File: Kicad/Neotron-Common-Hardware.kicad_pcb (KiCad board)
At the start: 4 copper layers, 243.8 x 243.8 mm, 197 parts, among them J1001 SD_Card, J201 DE15HD, J301 RJ45_Amphenol_RJMG1BD3B8K1ANR, J401 CD Audio In, J402 AC'97 Audio Header, J403 Line Out, J501 USB Ports External, J502 USB Ports Internal, J601 Jack-DC, J602 Conn_01x04, J603 Double-mini-DIN-6, J801 Conn_02x05, J802 DB9_Male_MountingHoles, J901 DB9_Female_MountingHoles, SW601 SW_DIP_x01, SW602 SW_DIP_x01, U201 TPF133A, U202 TPD7S019, U301 ENC424J600-PT, U401 TLV320AIC23BPW, U402 STX-4335-5BGP-S1, U501 AP2501, U502 MIC2005A-2YM5, U503 MIC2005A-2YM5, U504 XR22404CG28, U505 MIC2005A-2YM5, U506 MIC2005A-2YM5, U601 K7805-3AR3, U602 AMS1117CD-3.3, U603 MAX1615xUK, U604 MKE04P24M48SF0, U801 ST3232CDR, Y301 25M, Y401 12M, Y501 12M

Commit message: Updated PCB
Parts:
- C601, C602: value 100u -> 100u 50V
- C606: value 1u -> 1u 50V
- F601: value 5A Polyfuse -> 6A PTC; footprint Fuse:Fuse_Littelfuse_395Series -> Fuse:Fuse_Bourns_MF-RG500
- J301: value RJ45_Amphenol_RJMG1BD3B8K1ANR -> RJ45 MagJack
- R209: value DNP -> DNF
- U201: value TPF133A -> THS7316
- U301: value ENC424J600-PT -> ENC424J600
- U601: value K7805-3AR3 -> 5V DC-DC Module
- U602: value AMS1117CD-3.3 -> 3v3 LDO
- U603: value MAX1615xUK -> MAX1615
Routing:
- net Net-(U504-Pad21): track 0.00 -> 1.24 mm, vias 0 -> 1
- net (no net): track 1.24 -> 0.00 mm, vias 1 -> 0

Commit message: Make CPU card bigger.
Just big enough to take a TQFP-176 now.
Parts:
- removed J901: DB9_Female_MountingHoles, Connector_Dsub:DSUB-9_Female_Horizontal_P2.77x2.84mm_EdgePinOffset4.94mm_Housed_MountingHolesOffset7.48mm
- removed R505: 100k, Resistor_SMD:R_0805_2012Metric_Pad1.15x1.40mm_HandSolder
- added C511: 4u7, Capacitor_THT:CP_Radial_D6.3mm_P2.50mm, F.Cu at (117.1, 50.2)
- added R507: 10k, Resistor_SMD:R_0805_2012Metric_Pad1.15x1.40mm_HandSolder, F.Cu at (124.6, 50.7)
- added R508: 10k, Resistor_SMD:R_0805_2012Metric_Pad1.15x1.40mm_HandSolder, F.Cu at (123.9, 42.6)
- added R509: 10k, Resistor_SMD:R_0805_2012Metric_Pad1.15x1.40mm_HandSolder, F.Cu at (124.6, 53.7)
- added U101: Neotron-CPU, Neotron-Common-Hardware:Neotron_CPU_Socket, F.Cu at (252.2, 163.3)
- moved C508 131.5 mm to (124.6, 47.8)
- moved C801 1.27 mm to (196.8, 70.5)
- moved J601 0.51 mm to (252.2, 43.4)
- moved U505 0.32 mm to (257.2, 62.9)
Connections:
- net /Video/BLUE renamed /Video/BLUE_ANA
- net /Video/GREEN renamed /Video/GREEN_ANA
- net /Video/RED renamed /Video/RED_ANA
- C508 pad 1: Net-(C508-Pad1) -> /USB/USB_3V3
- R504 pad 1: /USB/USB_5V -> /USB/USB_3V3
- R504 pad 2: Net-(C508-Pad1) -> Net-(R504-Pad2)
- U504 pad 17: (no net) -> Net-(R504-Pad2)
- U504 pad 18: Net-(C508-Pad1) -> Net-(R508-Pad2)
- U504 pad 19: +3V3 -> Net-(R507-Pad2)
- U504 pad 21: (no net) -> /USB/USB_3V3
- U504 pad 27: +3V3 -> Net-(R509-Pad2)
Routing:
- net +3V3: track 4.74 -> 0.11 mm, vias 3 -> 0
- net GND: track 2.08 -> 0.00 mm, vias 1 -> 0
- net Net-(R507-Pad2): track 0.00 -> 1.24 mm, vias 0 -> 1
- net Net-(U504-Pad21): track 1.24 -> 0.00 mm, vias 1 -> 0
- net Net-(R509-Pad2): track 0.00 -> 1.24 mm, vias 0 -> 1
- net /USB/USB_3V3: track 0.00 -> 1.24 mm, vias 0 -> 1
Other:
- board text added: "DC In"
- board text added: "Ethernet"
- board text removed: "Ethernet 100base-T"

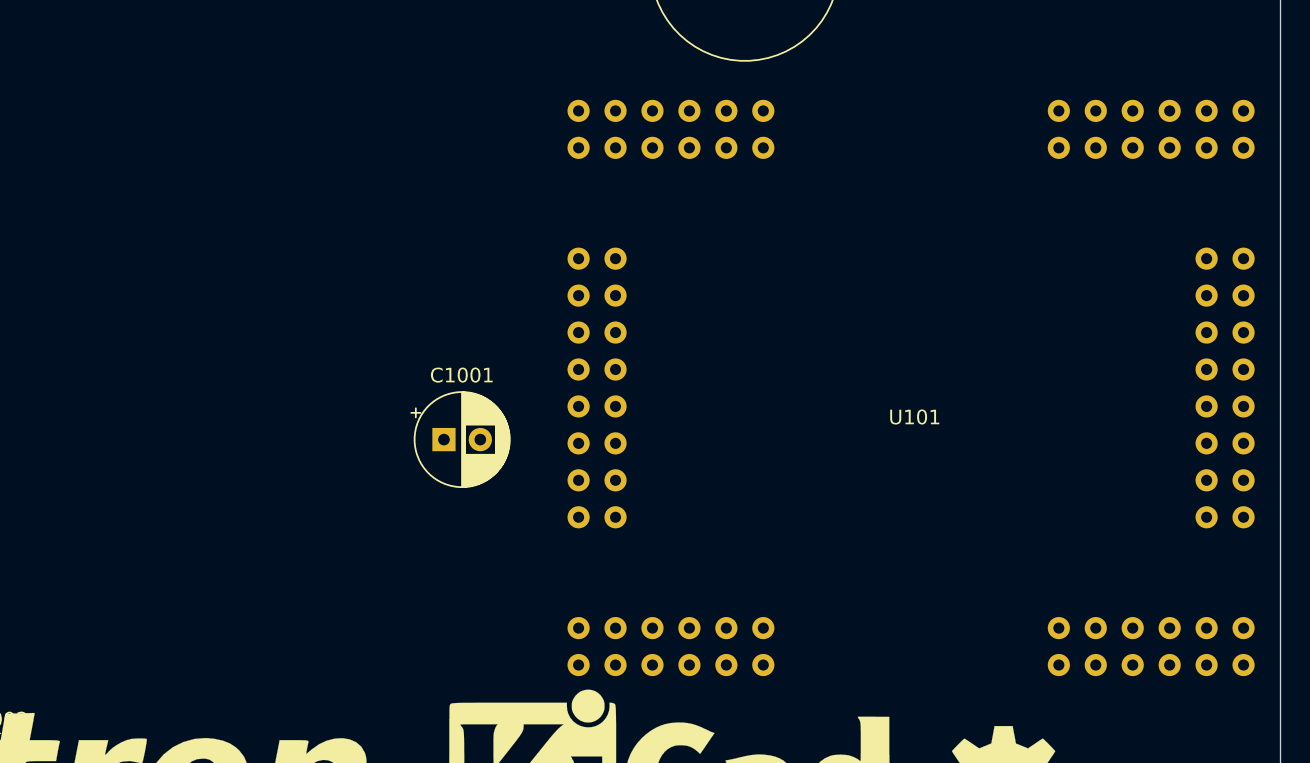
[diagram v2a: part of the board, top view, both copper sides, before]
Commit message: Revised CPU connector to be two 2x20.
This gives more room for larger TQFP-176+ CPUs to be fitted that
didn't fit on the PGA-80 design.
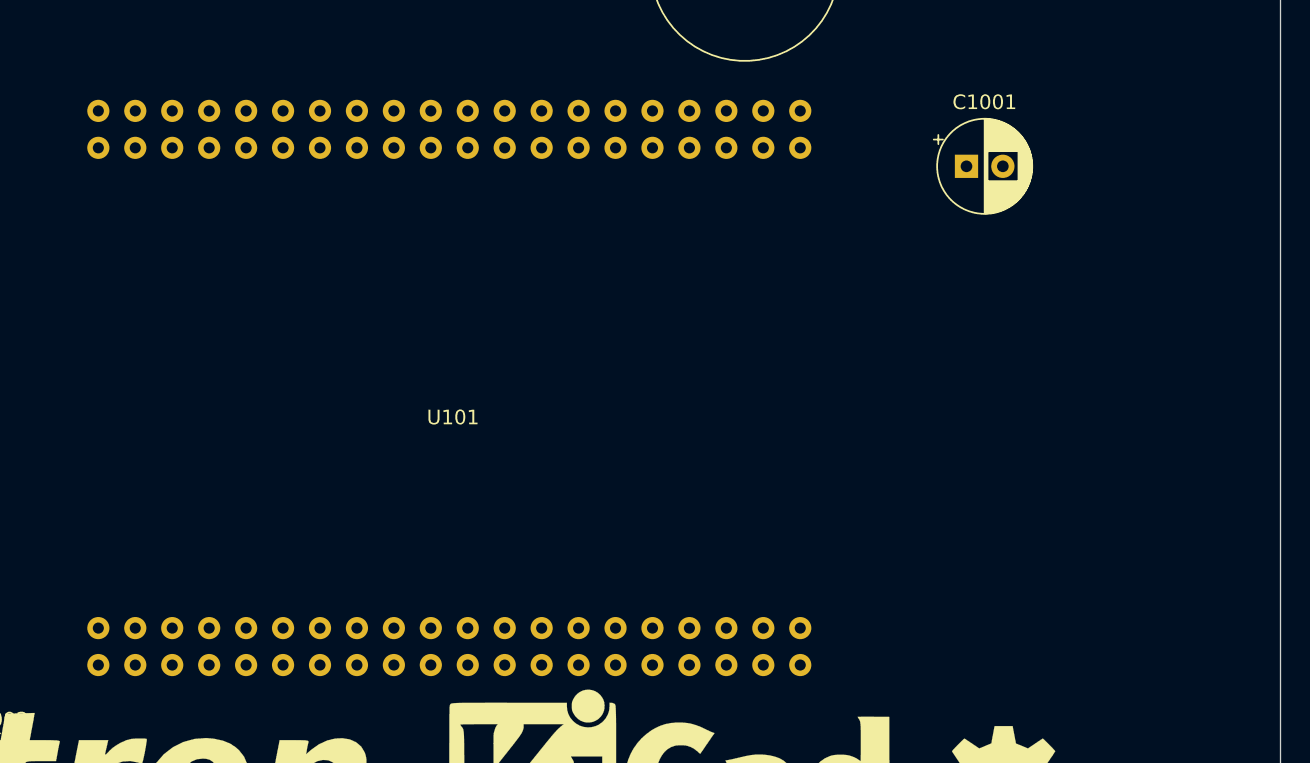
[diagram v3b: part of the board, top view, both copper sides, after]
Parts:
- moved C1001 40.5 mm to (256.0, 148.0)
- moved U101 31.8 mm to (220.4, 163.3)
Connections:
- net /Ethernet/~INT renamed /Ethernet/~IRQ

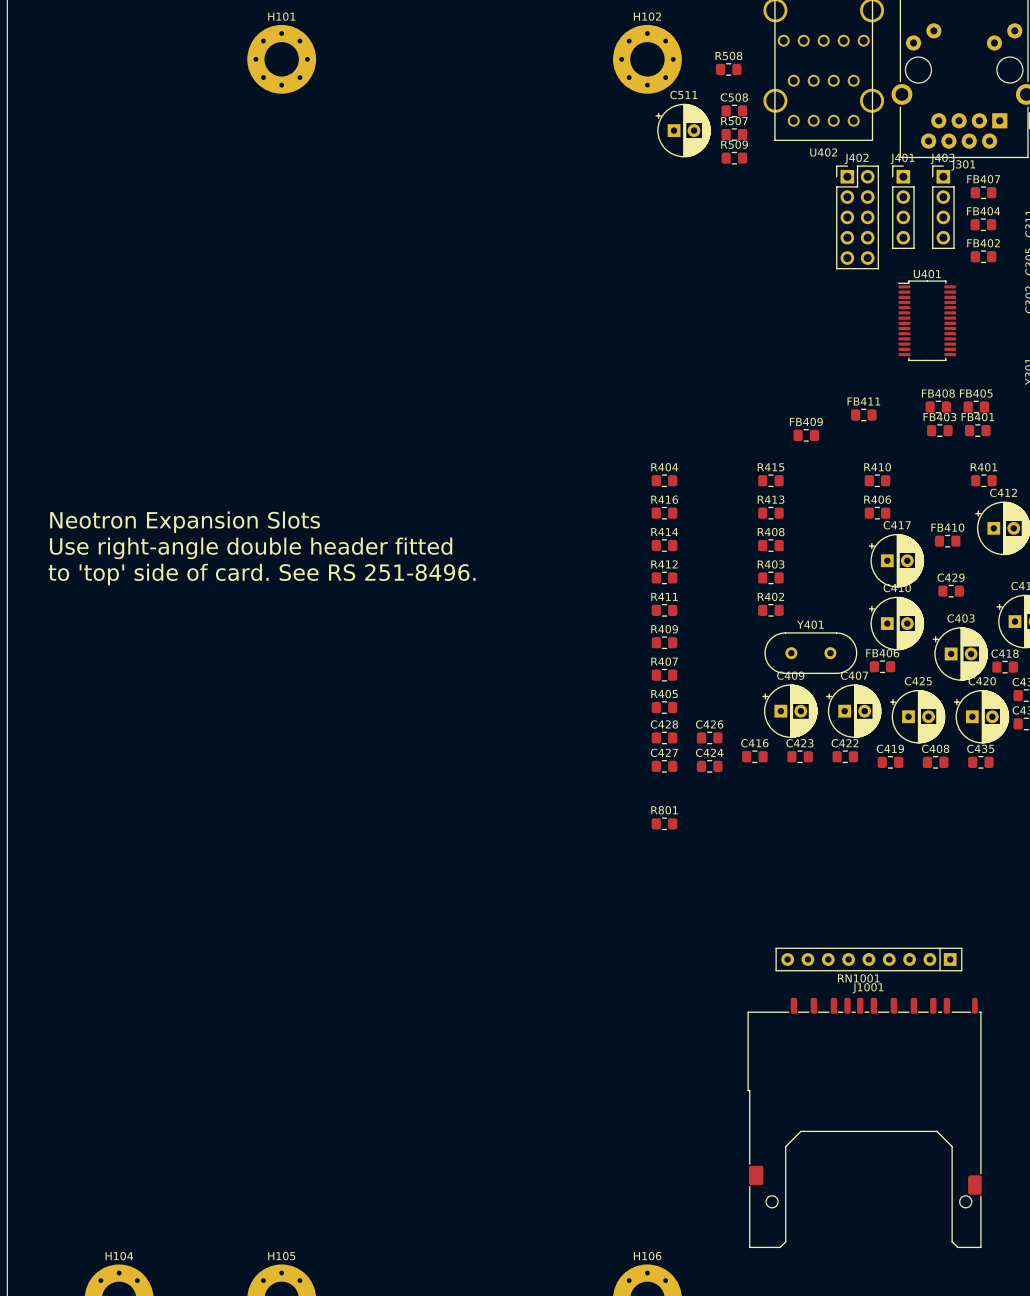
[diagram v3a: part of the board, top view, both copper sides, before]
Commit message: Changed CPU socket to be 2x20 x2. Added expansion slots.
Also added 3D model for the SD card.
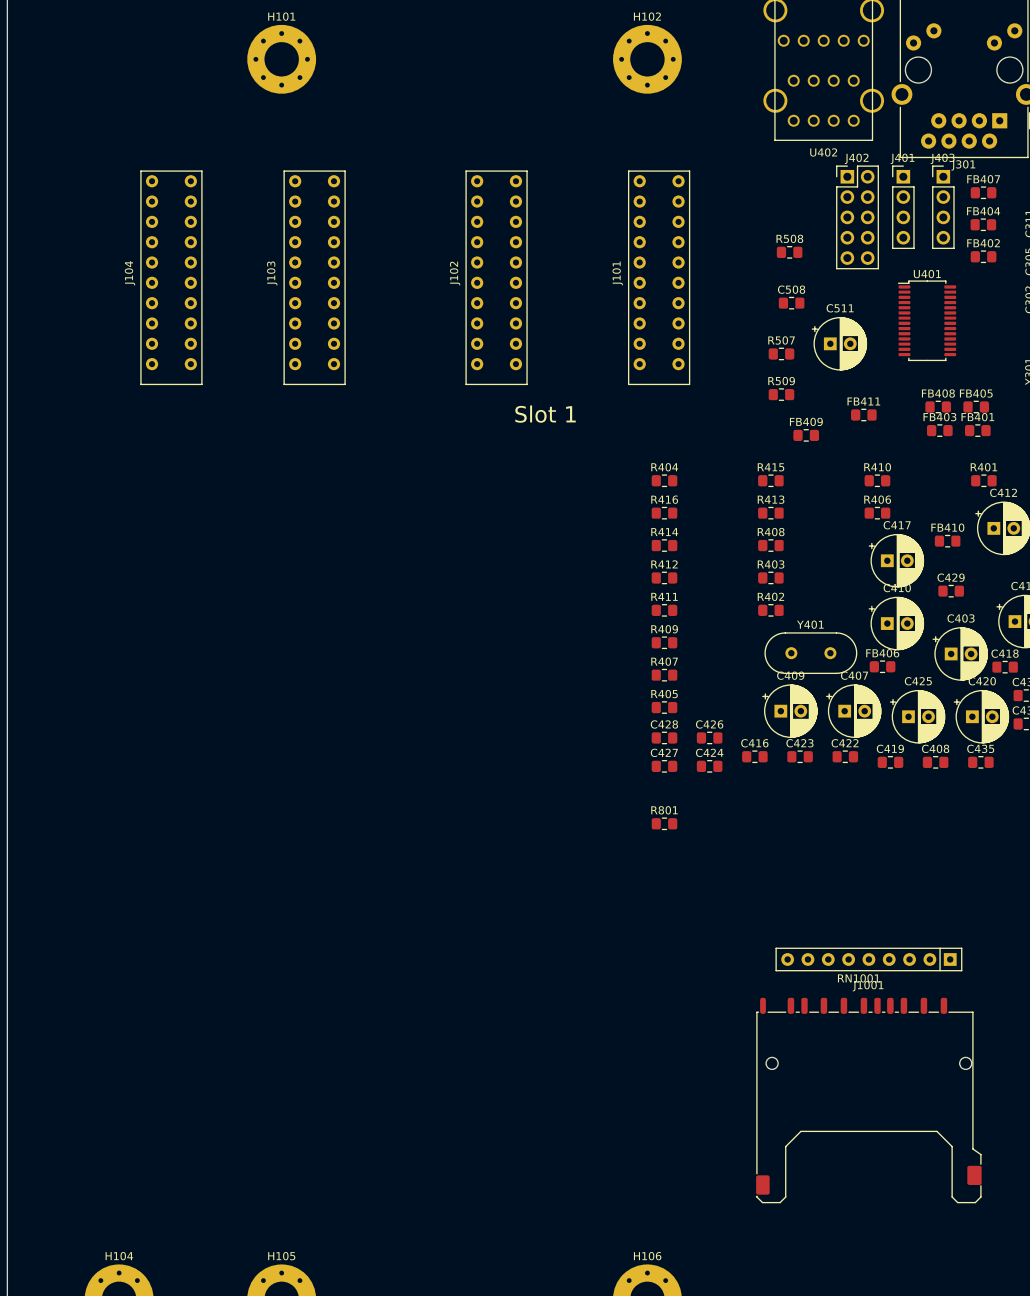
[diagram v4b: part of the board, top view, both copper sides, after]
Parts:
- added J101: Neotron-Expansion-Slot, Neotron-Common-Hardware:Neotron-Expansion-Slot, F.Cu at (115.2, 56.6)
- added J102: Neotron-Expansion-Slot, Neotron-Common-Hardware:Neotron-Expansion-Slot, F.Cu at (94.9, 56.6)
- added J103: Neotron-Expansion-Slot, Neotron-Common-Hardware:Neotron-Expansion-Slot, F.Cu at (72.2, 56.6)
- added J104: Neotron-Expansion-Slot, Neotron-Common-Hardware:Neotron-Expansion-Slot, F.Cu at (54.3, 56.6)
- J1001: footprint Connector_Card:SD_Kyocera_145638109511859+ -> Connector_Card:SD_Kyocera_145638009211859+
- moved C511 33.0 mm to (136.6, 76.9)
- moved R509 30.1 mm to (130.5, 83.2)
- moved R507 28.0 mm to (130.5, 78.2)
- moved C508 25.1 mm to (131.8, 71.8)
- moved R508 24.1 mm to (131.6, 65.5)
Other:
- board text added: "Cards are at 0.800" centres. NOTE: They are the "PCI" way around, i.e. components to the left, NOT the "ISA" way around. This is so a single slot fits on an ITX board."
- board text added: "Slot 1"
- board text removed: "Neotron Expansion Slots Use right-angle double header fitted to 'top' side of card. See RS 251-8496."

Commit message: Rejigged expansion socket, and added pinout to README.
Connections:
- J101 pad 14: GND -> (no net)
- J101 pad 17: GND -> +3V3
- J101 pad 20: +3V3 -> GND
- J102 pad 14: GND -> (no net)
- J102 pad 17: GND -> +3V3
- J102 pad 20: +3V3 -> GND
- J103 pad 14: GND -> (no net)
- J103 pad 17: GND -> +3V3
- J103 pad 20: +3V3 -> GND
- J104 pad 14: GND -> (no net)
- J104 pad 17: GND -> +3V3
- J104 pad 20: +3V3 -> GND

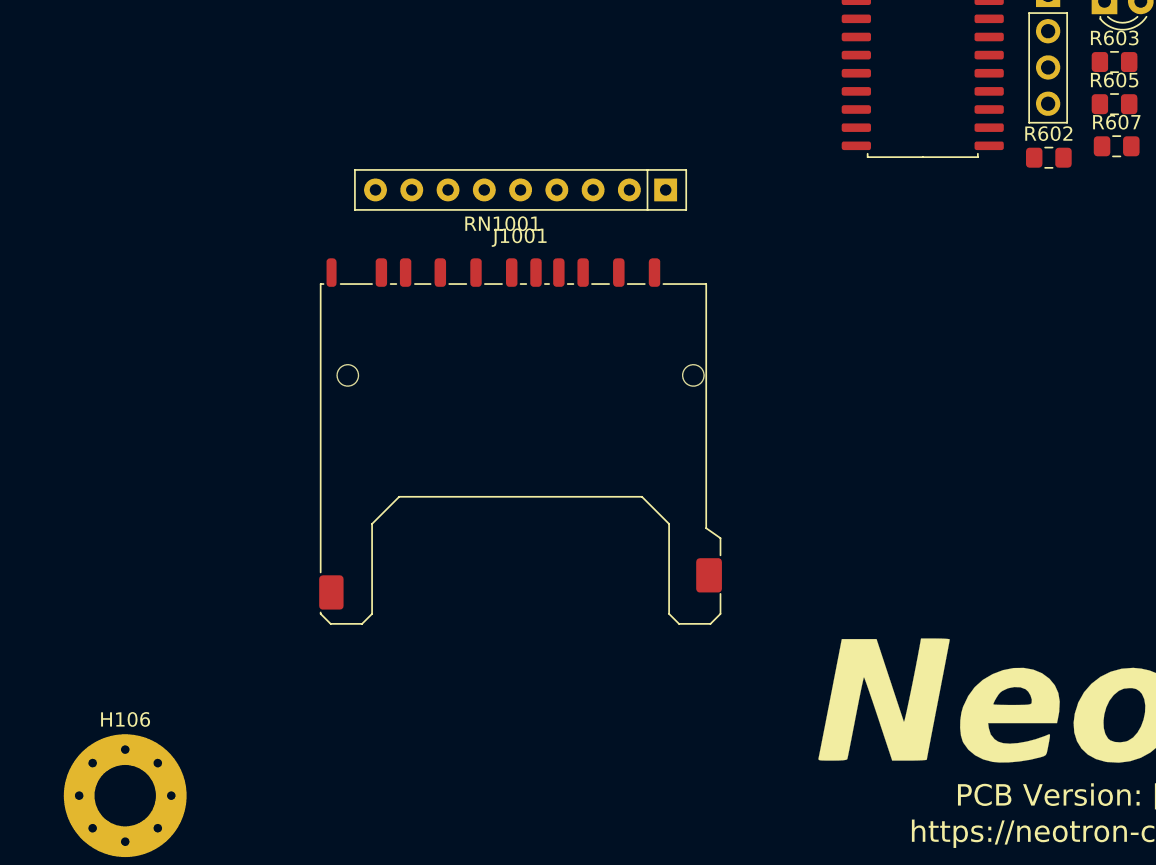
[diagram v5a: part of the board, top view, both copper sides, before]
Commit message: Add real-time clock.
I copied the MCP7940N design from the Neotron-32 but changed
the chip to a SOIC-8.
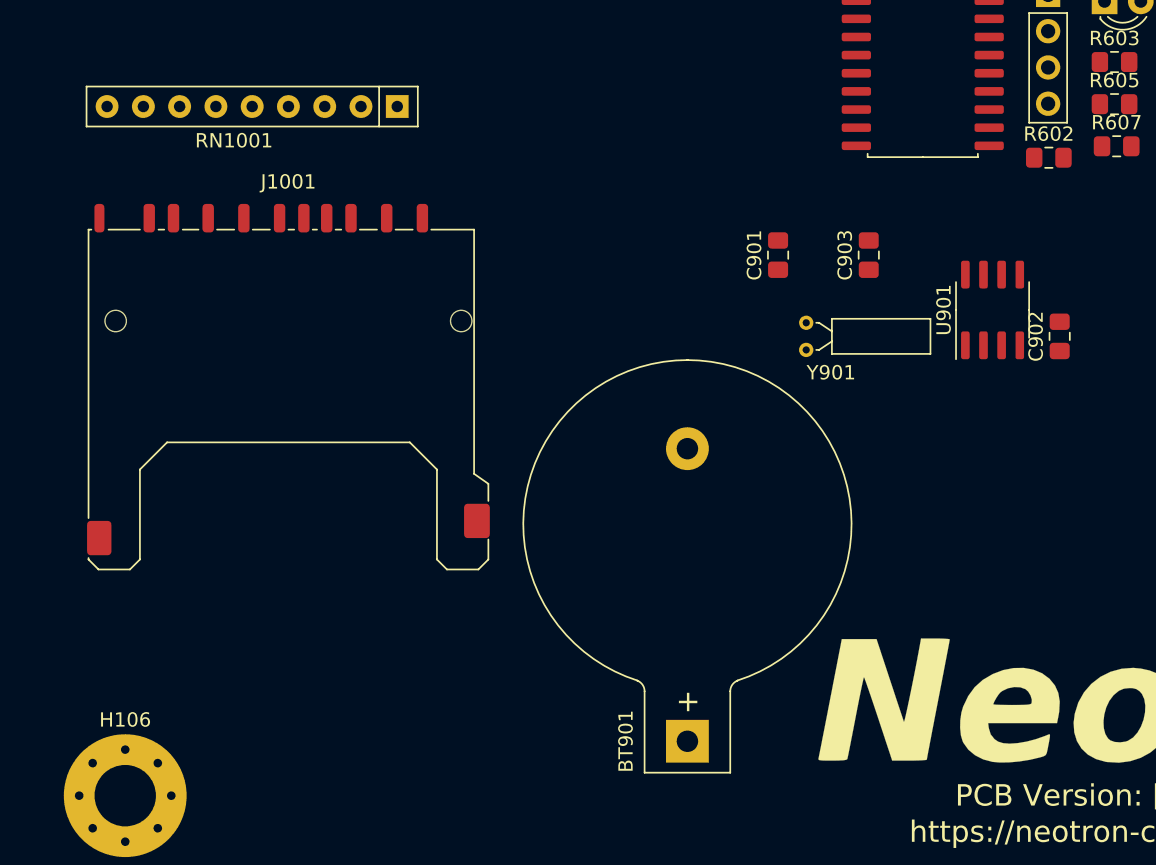
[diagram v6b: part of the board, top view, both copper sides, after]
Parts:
- added BT901: Coin Cell, Neotron-Common-Hardware:BatteryHolder_Keystone_103_1x20mm, F.Cu at (153.1, 192.5)
- added C901: 100n, Capacitor_SMD:C_0805_2012Metric_Pad1.15x1.40mm_HandSolder, F.Cu at (159.5, 158.4)
- added C902: 6p, Capacitor_SMD:C_0805_2012Metric_Pad1.15x1.40mm_HandSolder, F.Cu at (179.2, 164.1)
- added C903: 6p, Capacitor_SMD:C_0805_2012Metric_Pad1.15x1.40mm_HandSolder, F.Cu at (165.8, 158.4)
- added U901: MCP7940, Package_SO:SOIC-8_3.9x4.9mm_P1.27mm, F.Cu at (174.5, 162.3)
- added Y901: 32,768 Hz, Crystal:Crystal_C26-LF_D2.1mm_L6.5mm_Horizontal, F.Cu at (161.5, 165.1)
- moved RN1001 19.7 mm to (132.8, 148.0)
- moved J1001 16.7 mm to (125.2, 168.3)
